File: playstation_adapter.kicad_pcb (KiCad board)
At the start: 2 copper layers, 21.1 x 45.7 mm, 34 parts, among them J1 Conn_01x03, J2 Conn_01x13, J3 GT-USB-7047C, SW1 SW_Push, U1 XC6206P332MR, U2 SRV05-4, U3 RP2040, U4 W25QXXXJV, Y1 X322512MSB4SI

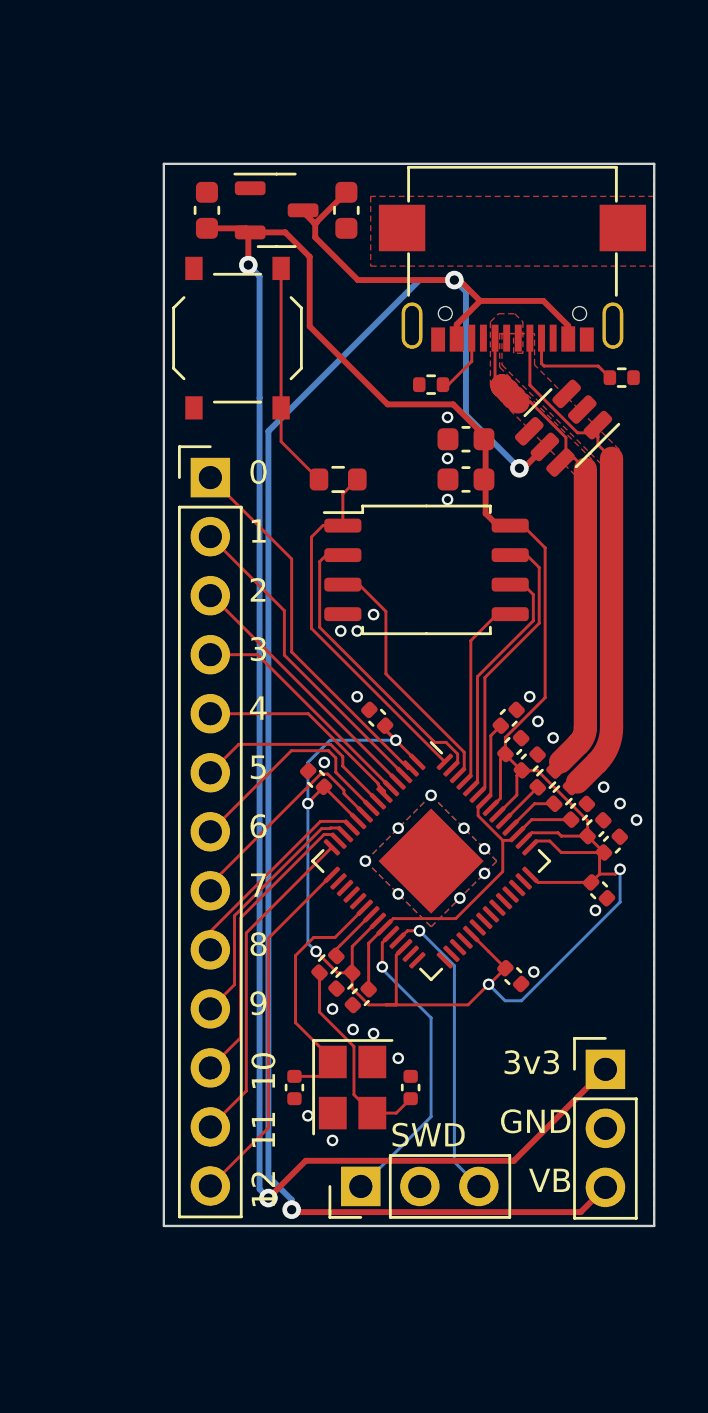
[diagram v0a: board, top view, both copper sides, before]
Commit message: Modified example pcb to playstation adapter pcb
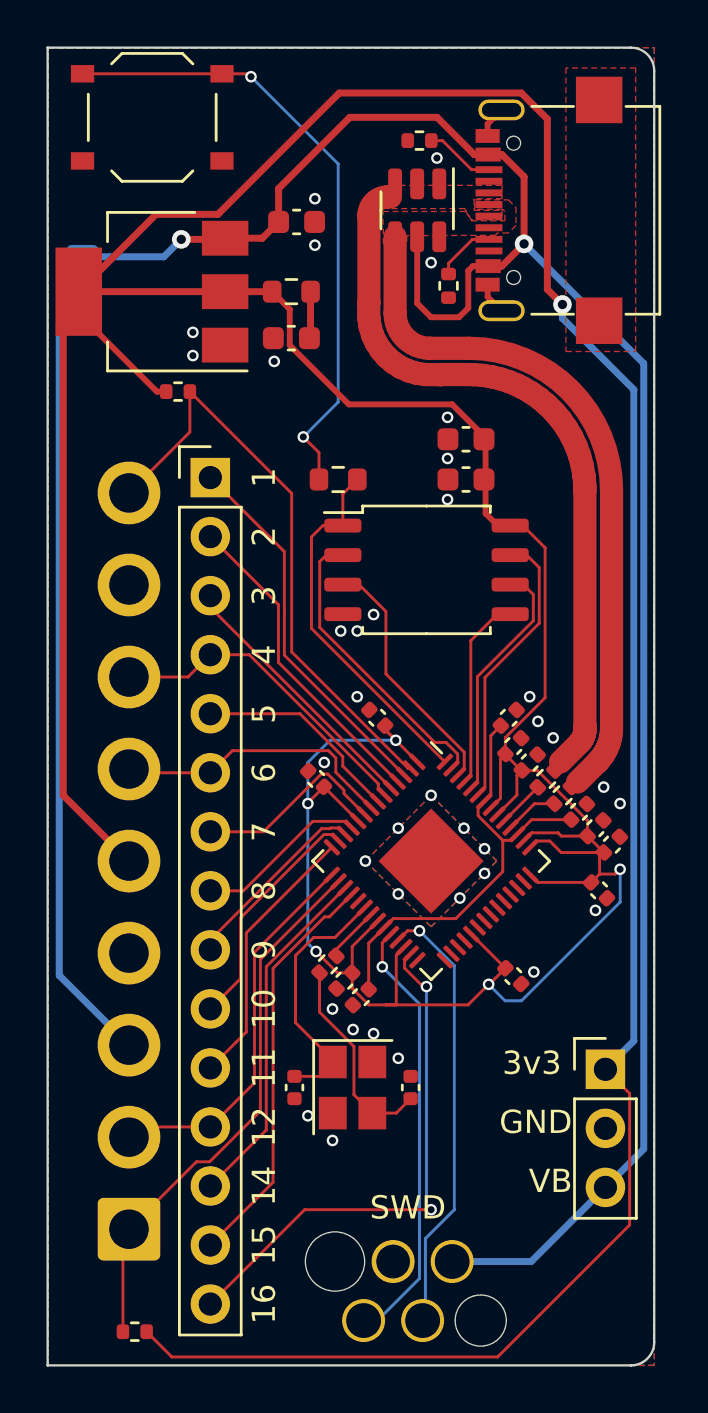
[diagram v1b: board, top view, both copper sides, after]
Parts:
- added J4: ~, footprints:PSX port, B.Cu at (67.5, 72.0)
- added R1: 1R, Resistor_SMD:R_0603_1608Metric, F.Cu at (66.0, 47.5)
- added R10: 1k5, Resistor_SMD:R_0402_1005Metric, F.Cu at (61.1, 51.8)
- added R2: 0, DNF, Resistor_SMD:R_0805_2012Metric, B.Cu at (57.0, 46.9)
- added R9: 1k5, Resistor_SMD:R_0402_1005Metric, F.Cu at (59.2, 92.2)
- C2: value 1u -> 22u
- J2: footprint Connector_PinHeader_2.54mm:PinHeader_1x13_P2.54mm_Vertical -> footprints:PinHeader_1x15_P2.54mm_Vertical_no_courtyard
- SWD1: value Conn_01x03 -> Conn_01x04; footprint Connector_PinHeader_2.54mm:PinHeader_1x03_P2.54mm_Vertical -> footprints:REDFIT 4 pin
- U1: value XC6206P332MR -> AMS1117-3.3; footprint footprints:SOT-23-3_flipped_for_jlcpcb -> footprints:SOT-223-3_TabPin2_flipped_for_jlcpcb
- moved U2 11.3 mm to (71.4, 44.0), turned to 90 degrees
- moved R8 10.5 mm to (71.5, 41.0)
- moved SW1 10.2 mm to (60.0, 40.0), turned to 180 degrees
- moved R7 8.43 mm to (72.8, 47.2), turned to -90 degrees
- moved C2 6.59 mm to (66.0, 49.5), turned to 180 degrees
- moved U1 6.41 mm to (60.0, 47.5), turned to 0 degrees
- moved SWD1 4.93 mm to (71.0, 90.5), turned to 180 degrees
- moved J3 3.35 mm to (77.0, 44.0), turned to 90 degrees
- moved C1 2.20 mm to (66.2, 44.5), turned to 0 degrees
- renumbered R1 to R7, R2 to R8
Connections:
- C2 pad 1: +3V3 -> Net-(C2-Pad1)
- J2 pad 1: /RP2040-base/GPIO0 -> /RP2040-base/GPIO1
- J2 pad 10: /RP2040-base/GPIO9 -> /RP2040-base/GPIO10
- J2 pad 11: /RP2040-base/GPIO10 -> /RP2040-base/GPIO11
- J2 pad 12: /RP2040-base/GPIO11 -> /RP2040-base/GPIO12
- J2 pad 13: /RP2040-base/GPIO12 -> /RP2040-base/GPIO14
- J2 pad 2: /RP2040-base/GPIO1 -> /RP2040-base/GPIO2
- J2 pad 3: /RP2040-base/GPIO2 -> /RP2040-base/GPIO3
- J2 pad 4: /RP2040-base/GPIO3 -> /RP2040-base/GPIO4
- J2 pad 5: /RP2040-base/GPIO4 -> /RP2040-base/GPIO5
- J2 pad 6: /RP2040-base/GPIO5 -> /RP2040-base/GPIO6
- J2 pad 7: /RP2040-base/GPIO6 -> /RP2040-base/GPIO7
- J2 pad 8: /RP2040-base/GPIO7 -> /RP2040-base/GPIO8
- J2 pad 9: /RP2040-base/GPIO8 -> /RP2040-base/GPIO9
- U2 pad 1: /RP2040-base/USB_D- -> GND
- U2 pad 3: GND -> /RP2040-base/USB_D+
- U2 pad 4: GND -> /RP2040-base/USB_D-
- U2 pad 6: /RP2040-base/USB_D+ -> GND
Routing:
- net +3V3: track 160.7 -> 235.4 mm, vias 7 -> 6
- net /vibrator power: track 0.00 -> 33.8 mm
- net /RP2040-base/GPIO13: track 0.00 -> 23.7 mm
- net /RP2040-base/GPIO16: track 0.00 -> 22.9 mm, vias 0 -> 2
- net /RP2040-base/GPIO15: track 0.00 -> 17.7 mm
- net /RP2040-base/~{USB_BOOT}: track 9.76 -> 27.1 mm, vias 0 -> 2
- net /RP2040-base/GPIO14: track 0.00 -> 15.2 mm
- net /RP2040-base/USB_D+: track 21.2 -> 31.3 mm
- net /RP2040-base/GPIO0: track 16.2 -> 25.7 mm
- net /RP2040-base/USB_D-: track 22.1 -> 29.7 mm
- net /RP2040-base/SWD: track 13.2 -> 19.1 mm
- net /RP2040-base/SWCLK: track 13.2 -> 18.5 mm
- net /RP2040-base/GPIO4: track 9.06 -> 14.0 mm
- net GND: track 0.00 -> 2.74 mm, vias 30 -> 36
- net /RP2040-base/GPIO9: track 10.9 -> 8.33 mm
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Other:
- board size 21.1 x 45.7 mm -> 26.1 x 56.7 mm
- board text added: "14"
- board text added: "15"
- board text added: "16"
- board text removed: "0"
